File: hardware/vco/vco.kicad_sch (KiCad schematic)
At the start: 104 parts, among them J1 AudioJack2, J2 AudioJack2, J3 AudioJack2, J4 AudioJack2, J5 AudioJack2, J6 AudioJack2, J7 AudioJack2, J8 16 Pin IDC, Q1 BC557B, Q2 BC547B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

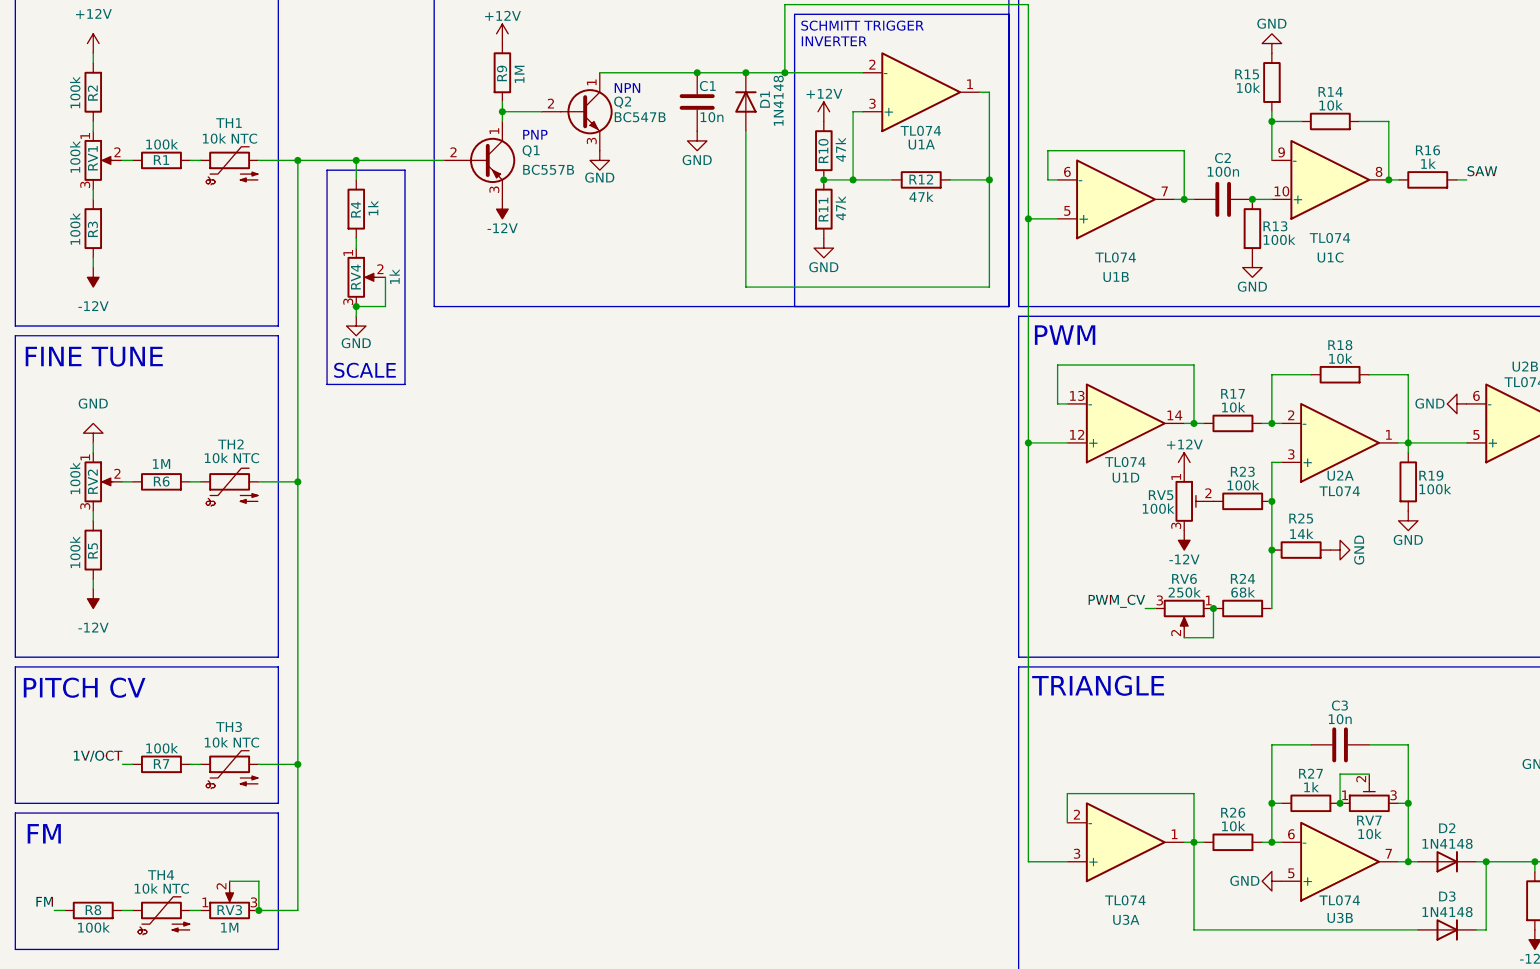
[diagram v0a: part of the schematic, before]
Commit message: start of tht version
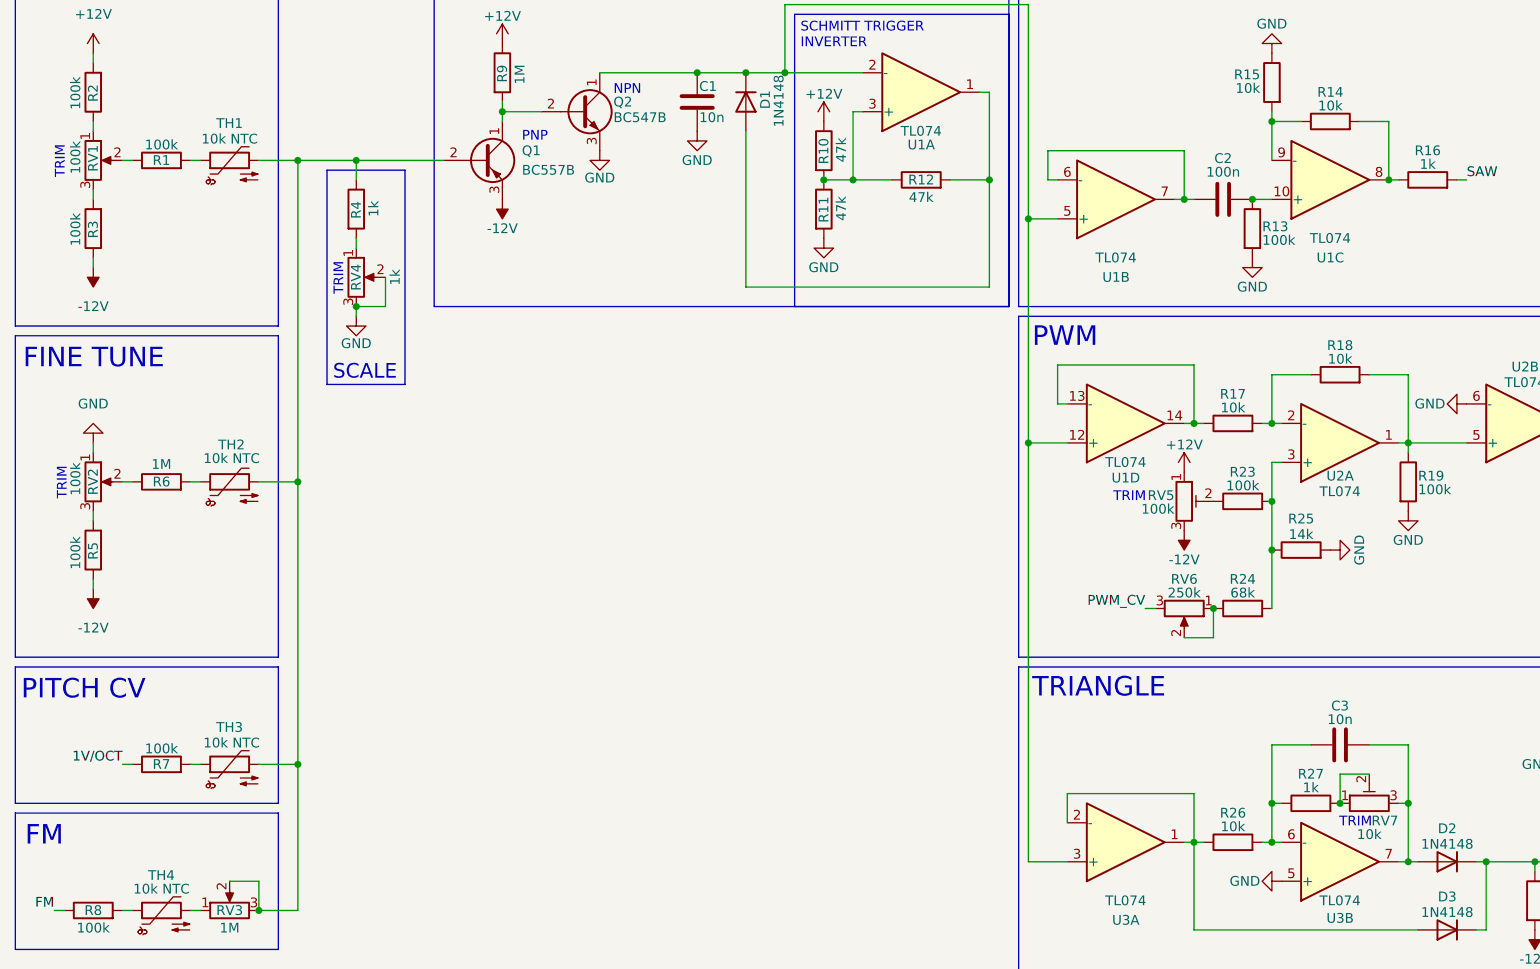
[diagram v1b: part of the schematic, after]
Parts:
- C1, C3: footprint (none) -> Capacitor_THT:C_Rect_L9.0mm_W3.3mm_P7.50mm_MKT
- C10, C2, C4, C5, C6, C7, C8, C9: footprint (none) -> Capacitor_THT:C_Rect_L9.0mm_W4.2mm_P7.50mm_MKT
- C11, C12: footprint (none) -> Capacitor_THT:CP_Radial_D4.0mm_P2.00mm
- J1, J2, J3, J4, J5, J6, J7: footprint (none) -> PJ301M-2-B:Jack_3.5mm_QingPu_WQP-PJ301M-12_Vertical
- J8: footprint (none) -> Connector_IDC:IDC-Header_2x08_P2.54mm_Vertical
- RV1, RV2, RV4, RV5, RV7: footprint (none) -> 3362P-1-253LF:TRIM_3362P-1-253LF
- RV3, RV6: footprint (none) -> RK097:Potentiometer_Alps_RK097_Single_Vertical
- TH1, TH2, TH3, TH4: footprint (none) -> Resistor_THT:R_Axial_DIN0204_L3.6mm_D1.6mm_P1.90mm_Vertical
- U1, U2, U3: footprint (none) -> Package_DIP:DIP-14_W7.62mm
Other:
- note added: "TRIM"
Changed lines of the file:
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@@
 		)
 	)
+	(text "TRIM"
+		(exclude_from_sim no)
+		(at 189.992 127 0)
+		(effects
+			(font
+				(size 1.27 1.27)
+			)
+		)
+	)
 	(text "3.5MM JACKS"
 		(exclude_from_sim no)
@@
 		)
 	)
+	(text "TRIM"
+		(exclude_from_sim no)
+		(at 21.082 40.894 90)
+		(effects
+			(font
+				(size 1.27 1.27)
+			)
+		)
+	)
+	(text "TRIM"
+		(exclude_from_sim no)
+		(at 57.404 56.134 90)
+		(effects
+			(font
+				(size 1.27 1.27)
+			)
+		)
+	)
 	(text "TRIANGLE"
 		(exclude_from_sim no)
@@
 		)
 	)
+	(text "TRIM"
+		(exclude_from_sim no)
+		(at 21.336 82.804 90)
+		(effects
+			(font
+				(size 1.27 1.27)
+			)
+		)
+	)
 	(text "SAWTOOTH OSCILLATOR CORE"
 		(exclude_from_sim no)
@@
 		)
 	)
+	(text "TRIM"
+		(exclude_from_sim no)
+		(at 160.528 84.582 0)
+		(effects
+			(font
+				(size 1.27 1.27)
+			)
+		)
+	)
 	(junction
 		(at 196.85 132.08)
@@
 			)
 		)
-		(property "Footprint" ""
+		(property "Footprint" "Capacitor_THT:C_Rect_L9.0mm_W4.2mm_P7.50mm_MKT"
 			(at 398.4752 31.75 0)
 			(hide yes)
@@
 			)
 		)
-		(property "Footprint" ""
+		(property "Footprint" "Package_DIP:DIP-14_W7.62mm"
 			(at 237.49 74.93 0)
 			(hide yes)
@@
 			)
 		)
-		(property "Footprint" ""
+		(property "Footprint" "Package_DIP:DIP-14_W7.62mm"
 			(at 186.69 80.01 0)
 			(hide yes)
@@
 			)
 		)
-		(property "Footprint" ""
+		(property "Footprint" "Resistor_THT:R_Axial_DIN0204_L3.6mm_D1.6mm_P1.90mm_Vertical"
 			(at 41.91 82.55 0)
 			(hide yes)
@@
 			)
 		)
-		(property "Footprint" ""
+		(property "Footprint" "Capacitor_THT:C_Rect_L9.0mm_W3.3mm_P7.50mm_MKT"
 			(at 191.77 115.8748 0)
 			(hide yes)
@@
 			)
 		)
-		(property "Footprint" ""
+		(property "Footprint" "Capacitor_THT:CP_Radial_D4.0mm_P2.00mm"
 			(at 393.7 99.06 0)
 			(hide yes)
@@
 			)
 		)
-		(property "Footprint" ""
+		(property "Footprint" "PJ301M-2-B:Jack_3.5mm_QingPu_WQP-PJ301M-12_Vertical"
 			(at 336.55 45.72 0)
 			(hide yes)
@@
 			)
 		)
-		(property "Footprint" ""
+		(property "Footprint" "Resistor_THT:R_Axial_DIN0204_L3.6mm_D1.6mm_P1.90mm_Vertical"
 			(at 41.91 119.38 0)
 			(hide yes)
@@
 			)
 		)
-		(property "Footprint" ""
+		(property "Footprint" "Package_DIP:DIP-14_W7.62mm"
 			(at 157.48 48.26 0)
 			(hide yes)
@@
 			)
 		)
-		(property "Footprint" ""
+		(property "Footprint" "Package_DIP:DIP-14_W7.62mm"
 			(at 185.42 45.72 0)
 			(hide yes)
@@
 			)
 		)
-		(property "Footprint" ""
+		(property "Footprint" "Capacitor_THT:CP_Radial_D4.0mm_P2.00mm"
 			(at 393.7 106.68 0)
 			(hide yes)
@@
 			)
 		)
-		(property "Footprint" ""
+		(property "Footprint" "Package_DIP:DIP-14_W7.62mm"
 			(at 210.82 77.47 0)
 			(hide yes)
@@
 			)
 		)
-		(property "Footprint" ""
+		(property "Footprint" "3362P-1-253LF:TRIM_3362P-1-253LF"
 			(at 25.4 40.64 0)
 			(hide yes)
@@
 			)
 		)
-		(property "Footprint" ""
+		(property "Footprint" "Connector_IDC:IDC-Header_2x08_P2.54mm_Vertical"
 			(at 365.76 68.58 0)
 			(hide yes)
@@
 			)
 		)
-		(property "Footprint" ""
+		(property "Footprint" "PJ301M-2-B:Jack_3.5mm_QingPu_WQP-PJ301M-12_Vertical"
 			(at 336.55 31.75 0)
 			(hide yes)
@@
 			)
 		)
-		(property "Footprint" ""
+		(property "Footprint" "Package_DIP:DIP-14_W7.62mm"
 			(at 234.95 132.08 0)
 			(hide yes)
@@
 			)
 		)
-		(property "Footprint" ""
+		(property "Footprint" "RK097:Potentiometer_Alps_RK097_Single_Vertical"
 			(at 167.64 99.06 0)
 			(hide yes)
@@
 			)
 		)
-		(property "Footprint" ""
+		(property "Footprint" "Capacitor_THT:C_Rect_L9.0mm_W4.2mm_P7.50mm_MKT"
 			(at 381.9652 39.37 0)
 			(hide yes)
@@
 			)
 		)
-		(property "Footprint" ""
+		(property "Footprint" "PJ301M-2-B:Jack_3.5mm_QingPu_WQP-PJ301M-12_Vertical"
 			(at 336.55 59.69 0)
 			(hide yes)
@@
 			)
 		)
-		(property "Footprint" ""
+		(property "Footprint" "RK097:Potentiometer_Alps_RK097_Single_Vertical"
 			(at 43.18 138.43 0)
 			(hide yes)
@@
 			)
 		)
-		(property "Footprint" ""
+		(property "Footprint" "Package_DIP:DIP-14_W7.62mm"
 			(at 132.08 34.29 0)
 			(hide yes)
@@
 			)
 		)
-		(property "Footprint" ""
+		(property "Footprint" "Resistor_THT:R_Axial_DIN0204_L3.6mm_D1.6mm_P1.90mm_Vertical"
 			(at 33.02 138.43 0)
 			(hide yes)
@@
 			)
 		)
-		(property "Footprint" ""
+		(property "Footprint" "Capacitor_THT:C_Rect_L9.0mm_W4.2mm_P7.50mm_MKT"
 			(at 381.9652 31.75 0)
 			(hide yes)
@@
 			)
 		)
-		(property "Footprint" ""
+		(property "Footprint" "Package_DIP:DIP-14_W7.62mm"
 			(at 388.62 29.21 0)
 			(hide yes)
@@
 			)
 		)
-		(property "Footprint" ""
+		(property "Footprint" "3362P-1-253LF:TRIM_3362P-1-253LF"
 			(at 25.4 82.55 0)
 			(hide yes)
@@
 			)
 		)
-		(property "Footprint" ""
+		(property "Footprint" "Resistor_THT:R_Axial_DIN0204_L3.6mm_D1.6mm_P1.90mm_Vertical"
 			(at 41.91 40.64 0)
 			(hide yes)
@@
 			)
 		)
-		(property "Footprint" ""
+		(property "Footprint" "Package_DIP:DIP-14_W7.62mm"
 			(at 354.33 29.21 0)
 			(hide yes)
@@
 			)
 		)
-		(property "Footprint" ""
+		(property "Footprint" "Capacitor_THT:C_Rect_L9.0mm_W4.2mm_P7.50mm_MKT"
 			(at 364.1852 39.37 0)
 			(hide yes)
@@
 			)
 		)
-		(property "Footprint" ""
+		(property "Footprint" "Package_DIP:DIP-14_W7.62mm"
 			(at 369.57 34.29 0)
 			(hide yes)
@@
 			)
 		)
-		(property "Footprint" ""
+		(property "Footprint" "Capacitor_THT:C_Rect_L9.0mm_W4.2mm_P7.50mm_MKT"
 			(at 222.25 131.1148 0)
 			(hide yes)
@@
 			)
 		)
-		(property "Footprint" ""
+		(property "Footprint" "Package_DIP:DIP-14_W7.62mm"
 			(at 158.75 132.08 0)
 			(hide yes)
@@
 			)
 		)
-		(property "Footprint" ""
+		(property "Footprint" "Capacitor_THT:C_Rect_L9.0mm_W4.2mm_P7.50mm_MKT"
 			(at 364.1852 31.75 0)
 			(hide yes)
@@
 		(dnp no)
 		(property "Reference" "RV7"
-			(at 191.77 126.746 90)
+			(at 193.802 126.746 90)
 			(show_name no)
 			(do_not_autoplace no)
@@
 			)
 		)
-		(property "Footprint" ""
+		(property "Footprint" "3362P-1-253LF:TRIM_3362P-1-253LF"
 			(at 191.77 124.46 0)
 			(hide yes)
@@
 			)
 		)
-		(property "Footprint" ""
+		(property "Footprint" "Package_DIP:DIP-14_W7.62mm"
 			(at 279.4 166.37 0)
 			(hide yes)
@@
 			)
 		)
-		(property "Footprint" ""
+		(property "Footprint" "PJ301M-2-B:Jack_3.5mm_QingPu_WQP-PJ301M-12_Vertical"
 			(at 336.55 73.66 0)
 			(hide yes)
@@
 			)
 		)
-		(property "Footprint" ""
+		(property "Footprint" "PJ301M-2-B:Jack_3.5mm_QingPu_WQP-PJ301M-12_Vertical"
 			(at 313.69 45.72 0)
 			(hide yes)
@@
 			)
 		)
-		(property "Footprint" ""
+		(property "Footprint" "Capacitor_THT:C_Rect_L9.0mm_W4.2mm_P7.50mm_MKT"
 			(at 176.53 44.7548 0)
 			(hide yes)
@@
 			)
 		)
-		(property "Footprint" ""
+		(property "Footprint" "Capacitor_THT:C_Rect_L9.0mm_W3.3mm_P7.50mm_MKT"
 			(at 105.1052 36.83 0)
 			(hide yes)
@@
 			)
 		)
-		(property "Footprint" ""
+		(property "Footprint" "Package_DIP:DIP-14_W7.62mm"
 			(at 186.69 134.62 0)
 			(hide yes)
@@
 			)
 		)
-		(property "Footprint" ""
+		(property "Footprint" "3362P-1-253LF:TRIM_3362P-1-253LF"
 			(at 167.64 85.09 0)
 			(hide yes)
@@
 			)
 		)
-		(property "Footprint" ""
+		(property "Footprint" "PJ301M-2-B:Jack_3.5mm_QingPu_WQP-PJ301M-12_Vertical"
 			(at 313.69 59.69 0)
 			(hide yes)
@@
 			)
 		)
-		(property "Footprint" ""
+		(property "Footprint" "Package_DIP:DIP-14_W7.62mm"
 			(at 158.75 77.47 0)
 			(hide yes)
@@
 			)
 		)
-		(property "Footprint" ""
+		(property "Footprint" "Capacitor_THT:C_Rect_L9.0mm_W4.2mm_P7.50mm_MKT"
 			(at 398.4752 39.37 0)
 			(hide yes)
@@
 			)
 		)
-		(property "Footprint" ""
+		(property "Footprint" "Package_DIP:DIP-14_W7.62mm"
 			(at 158.75 163.83 0)
 			(hide yes)
@@
 			)
 		)
-		(property "Footprint" ""
+		(property "Footprint" "3362P-1-253LF:TRIM_3362P-1-253LF"
 			(at 59.69 55.88 0)
 			(hide yes)
@@
 			)
 		)
-		(property "Footprint" ""
+		(property "Footprint" "PJ301M-2-B:Jack_3.5mm_QingPu_WQP-PJ301M-12_Vertical"
 			(at 313.69 31.75 0)
 			(hide yes)

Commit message: end of first layout att
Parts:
- added R54, R55, R56: 100k, Resistor_THT:R_Axial_DIN0207_L6.3mm_D2.5mm_P2.54mm_Vertical, symbol Device:R
- added RV8: 100k, Potentiometer_THT:Potentiometer_Alps_RK09L_Single_Vertical, symbol Device:R_Potentiometer
- added TH5: 10k NTC, Resistor_THT:R_Axial_DIN0204_L3.6mm_D1.6mm_P1.90mm_Vertical, symbol Device:Thermistor_NTC
- RV3, RV6: footprint RK097:Potentiometer_Alps_RK097_Single_Vertical -> Potentiometer_THT:Potentiometer_Alps_RK09L_Single_Vertical
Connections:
- net +12V: now also R54.2
- net -12V: now also R55.1
- net at Q1.2 (B), R4.1, RV3.2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: now also TH5.2
- new net: R56.2, TH5.1
- new net: R55.2, RV8.3
- new net: R54.1, RV8.1
- new net: R56.1, RV8.2
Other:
- note added: "PITCH KNOB"

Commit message: Polish for submission
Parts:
- added C13: 10u, Capacitor_THT:CP_Radial_D4.0mm_P2.00mm, symbol Device:C_Polarized_US
- added C14: 22u, Capacitor_THT:CP_Radial_D4.0mm_P2.00mm, symbol Device:C_Polarized_US
- added C15: 10u, Capacitor_THT:CP_Radial_D4.0mm_P2.00mm, symbol Device:C_Polarized_Small_US
- added U4: AMS1117-2.5, Package_TO_SOT_SMD:SOT-223-3_TabPin2, symbol Regulator_Linear:AMS1117-2.5
- added U5: TC7660, TC7660:DIL08, symbol TC7660:TC7660
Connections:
- net +12V: now also C13.1, U4.3 (VI)
- net +2V5: now also C14.1, U4.2 (VO), U5.8 (V+)
- net -2V5: now also U5.5 (VOUT)
- net GND: now also C13.2, C14.2, U4.1 (GND), U5.3 (GND), U5.6 (LV)
- new net: C15.1, U5.2 (CAP+)
- new net: C15.2, U5.4 (CAP-)
- no-connect marks 2 -> 3
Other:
- note added: "LDO + CHARGE PUMP"
